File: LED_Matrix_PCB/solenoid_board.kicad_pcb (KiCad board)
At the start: 2 copper layers, 185 x 130 mm, 97 parts, among them J2 MCU_LEFT_LEGS, J3 MCU_RIGHT_LEGS

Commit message: Forgot to close files before pushing.
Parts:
- removed +5V_IN1: MCU_PWR_Supply, TerminalBlock:TerminalBlock_bornier-2_P5.08mm
- removed LED0_7, LED0_8, LED1_7, LED1_8, LED2_7, LED2_8, LED3_7, LED3_8, LED4_7, LED4_8, LED5_7, LED5_8, LED6_7, LED6_8, LED7_0, LED7_1, LED7_2, LED7_3, LED7_4, LED7_5, LED7_6, LED7_7, LED7_8: Screw-terminal, TerminalBlock:TerminalBlock_bornier-2_P5.08mm
- removed R330, R331, R332: 330, Resistor_THT:R_Axial_DIN0309_L9.0mm_D3.2mm_P20.32mm_Horizontal
- removed R333, R334, R335, R336, R337, R338: R, Resistor_THT:R_Axial_DIN0309_L9.0mm_D3.2mm_P20.32mm_Horizontal
- removed REF** (x4): MountingHole_2.7mm_M2.5, MountingHole:MountingHole_2.7mm_M2.5
- removed RJ0, RJ1: RJ45, Connector_RJ:RJ45_Amphenol_54602-x08_Horizontal
- added +5VIN1: Conn_01x02, Connector_PinHeader_2.54mm:PinHeader_1x02_P2.54mm_Vertical, F.Cu at (132.2, 74.0)
- added COMMS0: Conn_01x02, Connector_PinHeader_2.54mm:PinHeader_1x02_P2.54mm_Vertical, F.Cu at (103.2, 89.7)
- added COMMS1: Conn_01x02, Connector_PinHeader_2.54mm:PinHeader_1x02_P2.54mm_Vertical, F.Cu at (86.9, 108.6)
- added FET0: 2N7000, digikey-footprints:TO-92-3, F.Cu at (148.4, 89.1)
- added FET1: 2N7000, digikey-footprints:TO-92-3, F.Cu at (156.5, 81.9)
- added FET10: 2N7000, digikey-footprints:TO-92-3, F.Cu at (150.4, 99.7)
- added FET11: 2N7000, digikey-footprints:TO-92-3, F.Cu at (138.9, 114.1)
- added FET12: 2N7000, digikey-footprints:TO-92-3, F.Cu at (145.8, 108.8)
- added FET13: 2N7000, digikey-footprints:TO-92-3, F.Cu at (157.3, 97.8)
- added FET2: 2N7000, digikey-footprints:TO-92-3, F.Cu at (136.7, 103.5)
- added FET3: 2N7000, digikey-footprints:TO-92-3, F.Cu at (132.1, 110.7)
- added FET4: 2N7000, digikey-footprints:TO-92-3, F.Cu at (148.4, 94.4)
- added FET5: 2N7000, digikey-footprints:TO-92-3, F.Cu at (156.5, 87.2)
- added FET6: 2N7000, digikey-footprints:TO-92-3, F.Cu at (143.6, 103.5)
- added FET7: 2N7000, digikey-footprints:TO-92-3, F.Cu at (138.9, 108.8)
- added FET8: 2N7000, digikey-footprints:TO-92-3, F.Cu at (155.2, 92.5)
- added FET9: 2N7000, digikey-footprints:TO-92-3, F.Cu at (91.4, 114.3)
- added R10k0: 10k, Resistor_THT:R_Axial_DIN0204_L3.6mm_D1.6mm_P5.08mm_Vertical, F.Cu at (86.2, 95.3)
- added R10k1: 10k, Resistor_THT:R_Axial_DIN0204_L3.6mm_D1.6mm_P5.08mm_Vertical, F.Cu at (110.6, 73.2)
- added R10k10: 10k, Resistor_THT:R_Axial_DIN0204_L3.6mm_D1.6mm_P5.08mm_Vertical, F.Cu at (86.2, 82.7)
- added R10k11: 10k, Resistor_THT:R_Axial_DIN0204_L3.6mm_D1.6mm_P5.08mm_Vertical, F.Cu at (94.3, 76.4)
- added R10k12: 10k, Resistor_THT:R_Axial_DIN0204_L3.6mm_D1.6mm_P5.08mm_Vertical, F.Cu at (86.2, 79.5)
- added R10k13: 10k, Resistor_THT:R_Axial_DIN0204_L3.6mm_D1.6mm_P5.08mm_Vertical, F.Cu at (94.3, 73.2)
- added R10k2: 10k, Resistor_THT:R_Axial_DIN0204_L3.6mm_D1.6mm_P5.08mm_Vertical, F.Cu at (86.2, 76.4)
- added R10k3: 10k, Resistor_THT:R_Axial_DIN0204_L3.6mm_D1.6mm_P5.08mm_Vertical, F.Cu at (86.2, 73.2)
- added R10k4: 10k, Resistor_THT:R_Axial_DIN0204_L3.6mm_D1.6mm_P5.08mm_Vertical, F.Cu at (86.2, 89.0)
- added R10k5: 10k, Resistor_THT:R_Axial_DIN0204_L3.6mm_D1.6mm_P5.08mm_Vertical, F.Cu at (94.3, 82.7)
- added R10k6: 10k, Resistor_THT:R_Axial_DIN0204_L3.6mm_D1.6mm_P5.08mm_Vertical, F.Cu at (102.4, 76.4)
- added R10k7: 10k, Resistor_THT:R_Axial_DIN0204_L3.6mm_D1.6mm_P5.08mm_Vertical, F.Cu at (94.3, 79.5)
- added R10k8: 10k, Resistor_THT:R_Axial_DIN0204_L3.6mm_D1.6mm_P5.08mm_Vertical, F.Cu at (86.2, 85.8)
- added R10k9: 10k, Resistor_THT:R_Axial_DIN0204_L3.6mm_D1.6mm_P5.08mm_Vertical, F.Cu at (102.4, 73.2)
- added R300: 300, Resistor_THT:R_Axial_DIN0204_L3.6mm_D1.6mm_P5.08mm_Vertical, F.Cu at (110.6, 79.5)
- added R301: 300, Resistor_THT:R_Axial_DIN0204_L3.6mm_D1.6mm_P5.08mm_Vertical, F.Cu at (102.4, 85.8)
- added R302: 300, Resistor_THT:R_Axial_DIN0204_L3.6mm_D1.6mm_P5.08mm_Vertical, F.Cu at (86.2, 101.6)
- added R303: 300, Resistor_THT:R_Axial_DIN0204_L3.6mm_D1.6mm_P5.08mm_Vertical, F.Cu at (86.2, 92.1)
- added R304: 300, Resistor_THT:R_Axial_DIN0204_L3.6mm_D1.6mm_P5.08mm_Vertical, F.Cu at (86.2, 104.7)
- added R305: 300, Resistor_THT:R_Axial_DIN0204_L3.6mm_D1.6mm_P5.08mm_Vertical, F.Cu at (94.3, 95.3)
- added R306: 300, Resistor_THT:R_Axial_DIN0204_L3.6mm_D1.6mm_P5.08mm_Vertical, F.Cu at (118.7, 73.2)
- added R307: 300, Resistor_THT:R_Axial_DIN0204_L3.6mm_D1.6mm_P5.08mm_Vertical, F.Cu at (94.3, 92.1)
- added R308: 300, Resistor_THT:R_Axial_DIN0204_L3.6mm_D1.6mm_P5.08mm_Vertical, F.Cu at (86.2, 98.4)
- added R309: 300, Resistor_THT:R_Axial_DIN0204_L3.6mm_D1.6mm_P5.08mm_Vertical, F.Cu at (94.3, 89.0)
- added R310: 300, Resistor_THT:R_Axial_DIN0204_L3.6mm_D1.6mm_P5.08mm_Vertical, F.Cu at (102.4, 82.7)
- added R311: 300, Resistor_THT:R_Axial_DIN0204_L3.6mm_D1.6mm_P5.08mm_Vertical, F.Cu at (110.6, 76.4)
- added R312: 300, Resistor_THT:R_Axial_DIN0204_L3.6mm_D1.6mm_P5.08mm_Vertical, F.Cu at (102.4, 79.5)
- added R313: 300, Resistor_THT:R_Axial_DIN0204_L3.6mm_D1.6mm_P5.08mm_Vertical, F.Cu at (94.3, 85.8)
- GND1: value Conn_01x01_Male -> Conn_01x01
- LED0_0, LED0_1, LED0_2, LED0_3, LED0_4, LED0_5, LED0_6, LED1_0, LED1_1, LED1_2, LED1_3, LED1_4, LED1_5, LED1_6, LED2_0, LED2_1, LED2_2, LED2_3, LED2_4, LED2_5, LED2_6, LED3_0, LED3_1, LED3_2, LED3_3, LED3_4, LED3_5, LED3_6, LED4_0, LED4_1, LED4_2, LED4_3, LED4_4, LED4_5, LED4_6, LED5_0, LED5_1, LED5_2, LED5_3, LED5_4, LED5_5, LED5_6, LED6_0, LED6_1, LED6_2, LED6_3, LED6_4, LED6_5, LED6_6: value Screw-terminal -> Conn_01x02; footprint TerminalBlock:TerminalBlock_bornier-2_P5.08mm -> Connector_PinHeader_2.54mm:PinHeader_1x02_P2.54mm_Vertical
- R10, R11: footprint Resistor_THT:R_Axial_DIN0309_L9.0mm_D3.2mm_P20.32mm_Horizontal -> Resistor_THT:R_Axial_DIN0204_L3.6mm_D1.6mm_P7.62mm_Horizontal
- moved GND1 118.1 mm to (98.4, 113.6)
- moved LED0_0 99.9 mm to (160.1, 74.0)
- moved LED6_2 82.5 mm to (150.8, 74.0)
- moved LED5_0 77.5 mm to (136.9, 95.6)
- moved LED5_1 74.6 mm to (143.9, 88.4)
- moved LED4_0 71.9 mm to (127.6, 74.0)
- moved LED5_3 70.1 mm to (155.5, 74.0)
- moved LED0_1 68.4 mm to (118.3, 110.0)
- moved LED1_1 68.2 mm to (141.5, 74.0)
- moved LED4_1 67.2 mm to (139.2, 88.4)
- moved LED6_1 65.4 mm to (132.3, 95.6)
- moved LED2_1 63.7 mm to (136.9, 74.0)
- moved LED1_0 62.6 mm to (118.3, 95.6)
- moved LED0_2 61.6 mm to (142.7, 81.2)
- moved LED4_2 56.5 mm to (141.6, 95.6)
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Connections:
- net /RJ45_4 renamed /A
- net /RJ45_5 renamed /B
- J2 pad 11: /ROW6 -> (no net)
- J2 pad 12: /MOSI -> (no net)
- J3 pad 11: /SCL -> (no net)
- J3 pad 12: /SDA -> (no net)
- LED0_0 pad 2: /A0 -> /ROW0
- LED0_1 pad 2: /A0 -> /ROW0
- LED0_2 pad 2: /A0 -> /ROW0
- LED0_3 pad 2: /A0 -> /ROW0
- LED0_4 pad 2: /A0 -> /ROW0
- LED0_5 pad 2: /A0 -> /ROW0
- LED0_6 pad 2: /A0 -> /ROW0
- LED1_0 pad 2: /A1 -> /ROW1
- LED1_1 pad 2: /A1 -> /ROW1
- LED1_2 pad 2: /A1 -> /ROW1
- LED1_3 pad 2: /A1 -> /ROW1
- LED1_4 pad 2: /A1 -> /ROW1
- LED1_5 pad 2: /A1 -> /ROW1
- LED1_6 pad 2: /A1 -> /ROW1
- LED2_0 pad 2: /A2 -> /ROW2
- LED2_1 pad 2: /A2 -> /ROW2
- LED2_2 pad 2: /A2 -> /ROW2
- LED2_3 pad 2: /A2 -> /ROW2
- LED2_4 pad 2: /A2 -> /ROW2
- LED2_5 pad 2: /A2 -> /ROW2
- LED2_6 pad 2: /A2 -> /ROW2
- LED3_0 pad 2: /A3 -> /ROW3
- LED3_1 pad 2: /A3 -> /ROW3
- LED3_2 pad 2: /A3 -> /ROW3
- LED3_3 pad 2: /A3 -> /ROW3
- LED3_4 pad 2: /A3 -> /ROW3
- LED3_5 pad 2: /A3 -> /ROW3
- LED3_6 pad 2: /A3 -> /ROW3
- LED4_0 pad 2: /A4 -> /ROW4
- LED4_1 pad 2: /A4 -> /ROW4
- LED4_2 pad 2: /A4 -> /ROW4
- LED4_3 pad 2: /A4 -> /ROW4
- LED4_4 pad 2: /A4 -> /ROW4
- LED4_5 pad 2: /A4 -> /ROW4
- LED4_6 pad 2: /A4 -> /ROW4
- LED5_0 pad 2: /A5 -> /ROW5
- LED5_1 pad 2: /A5 -> /ROW5
- LED5_2 pad 2: /A5 -> /ROW5
- LED5_3 pad 2: /A5 -> /ROW5
- LED5_4 pad 2: /A5 -> /ROW5
- LED5_5 pad 2: /A5 -> /ROW5
- LED5_6 pad 2: /A5 -> /ROW5
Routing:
- net /A0: track 179.2 -> 0.00 mm
- net /MOSI: track 174.9 -> 0.00 mm
- net /D13: track 172.9 -> 0.00 mm
- net /A1: track 168.7 -> 0.00 mm
- net /ROW6: track 165.6 -> 0.00 mm
- net /A2: track 163.1 -> 0.00 mm
- net /D12: track 162.2 -> 0.00 mm
- net /A4: track 160.5 -> 0.00 mm
- net /A5: track 160.3 -> 0.00 mm
- net /A3: track 159.7 -> 0.00 mm
- net /D11: track 156.4 -> 0.00 mm
- net /D10: track 144.7 -> 0.00 mm
- net /D9: track 131.6 -> 0.00 mm
- net /D6: track 119.4 -> 0.00 mm
- net /D5: track 106.7 -> 0.00 mm
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- removed copper zone on B.Cu, net GND
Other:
- board outline removed
- board text added: "02/23/2020"
- board text added: "LED Matrix Board V2.0"
- board text removed: "02/07/2020"
- board text removed: "LED Matrix Board V1.0"

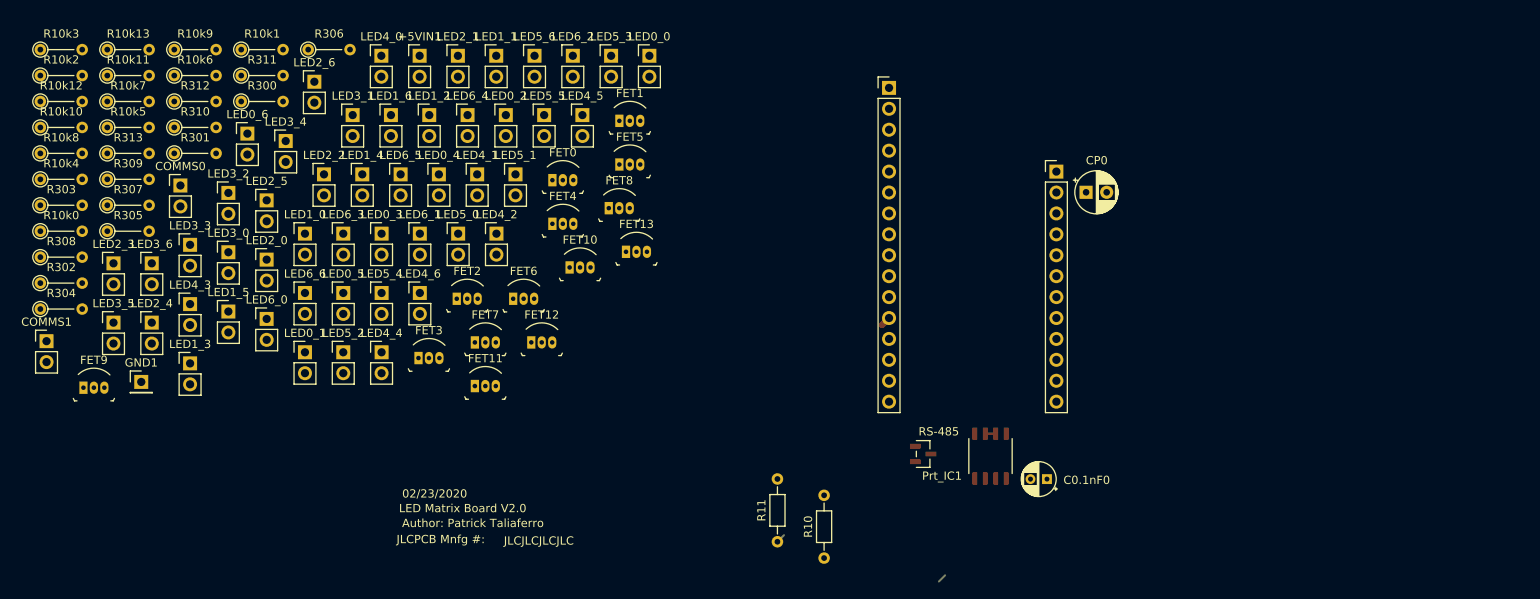
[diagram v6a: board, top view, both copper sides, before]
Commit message: Fixed the connections of the downstream MOSFETS. WOrked on geometry, sorted out footprints.
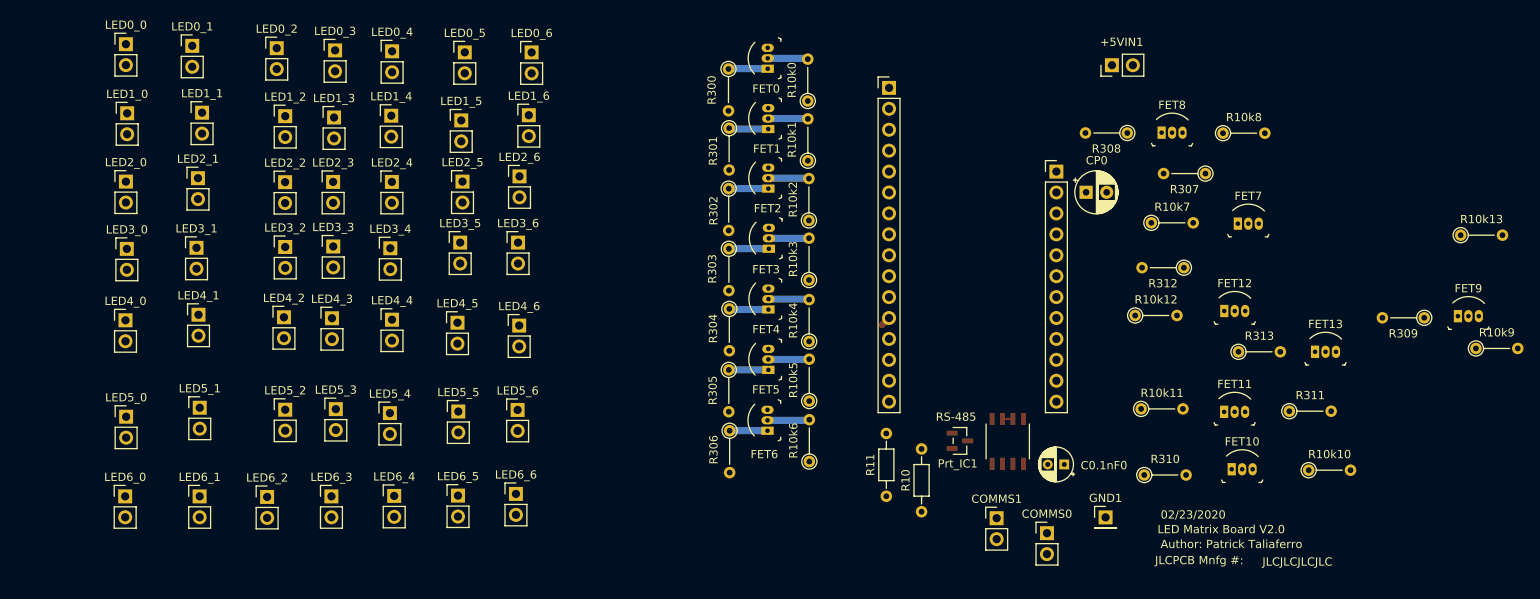
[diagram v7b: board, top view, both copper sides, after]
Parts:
- moved FET9 167.1 mm to (258.3, 105.6)
- moved R10k13 165.9 mm to (258.6, 95.7)
- moved R10k9 162.2 mm to (260.5, 109.5)
- moved R309 160.8 mm to (254.2, 105.8), turned to 180 degrees
- moved R10k10 159.5 mm to (240.2, 124.3)
- moved R10k8 143.6 mm to (229.8, 83.4)
- moved R313 139.4 mm to (231.7, 109.9)
- moved R10k12 135.4 mm to (219.1, 105.5)
- moved R311 133.6 mm to (237.8, 117.1)
- moved R307 133.4 mm to (227.6, 88.3), turned to 180 degrees
- moved R308 132.8 mm to (218.2, 83.3), turned to 180 degrees
- moved R10k11 131.9 mm to (219.8, 116.8)
- moved R10k7 127.6 mm to (221.1, 94.2)
- moved R310 125.1 mm to (220.2, 124.9)
- moved R312 124.2 mm to (225.0, 99.7), turned to 180 degrees
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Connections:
- FET10 pad 3: +5V -> /COL3
- FET11 pad 3: +5V -> /COL4
- FET12 pad 3: +5V -> /COL5
- FET13 pad 3: +5V -> /COL6
- FET7 pad 3: +5V -> /COL0
- FET8 pad 3: +5V -> /COL1
- FET9 pad 3: +5V -> /COL2
- R307 pad 2: /COL0 -> GND
- R308 pad 2: /COL1 -> GND
- R309 pad 2: /COL2 -> GND
- R310 pad 2: /COL3 -> GND
- R311 pad 2: /COL4 -> GND
- R312 pad 2: /COL5 -> GND
- R313 pad 2: /COL6 -> GND
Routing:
- net Net-(FET6-Pad2): track 0.00 -> 5.11 mm
- net Net-(FET5-Pad2): track 0.00 -> 4.98 mm
- net Net-(FET4-Pad2): track 0.00 -> 4.97 mm
- net Net-(FET2-Pad2): track 0.00 -> 4.95 mm
- net Net-(FET0-Pad2): track 0.00 -> 4.91 mm
- net Net-(FET3-Pad2): track 0.00 -> 4.88 mm
- net Net-(FET3-Pad1): track 0.00 -> 4.85 mm
- net Net-(FET1-Pad2): track 0.00 -> 4.83 mm
- net Net-(FET2-Pad1): track 0.00 -> 4.81 mm
- net Net-(FET5-Pad1): track 0.00 -> 4.80 mm
- net Net-(FET1-Pad1): track 0.00 -> 4.79 mm
- net Net-(FET4-Pad1): track 0.00 -> 4.78 mm
- net Net-(FET0-Pad1): track 0.00 -> 4.77 mm
- net Net-(FET6-Pad1): track 0.00 -> 4.60 mm
- net /B: track 2.19 -> 0.00 mm
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
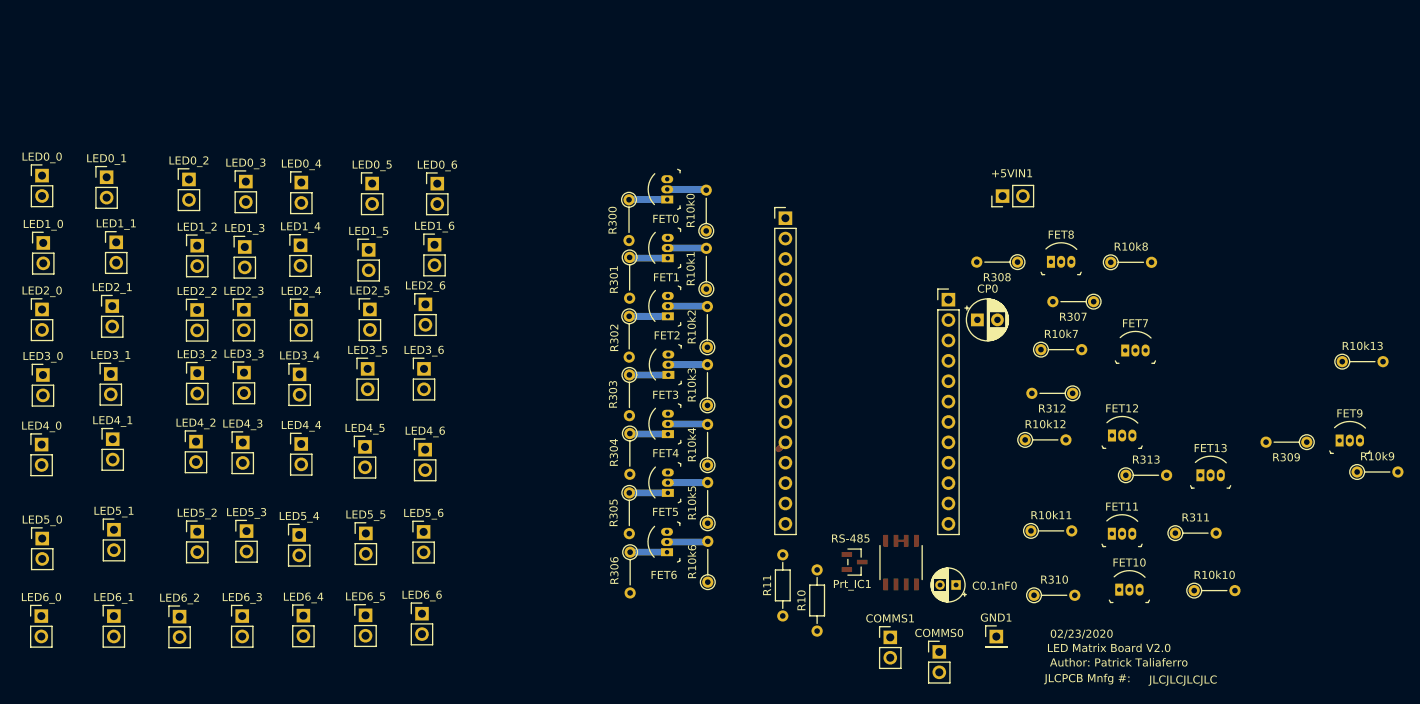
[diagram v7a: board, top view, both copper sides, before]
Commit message: Cleaned geometry on layout. Routed a number of wires. Only a little bit of routing left.
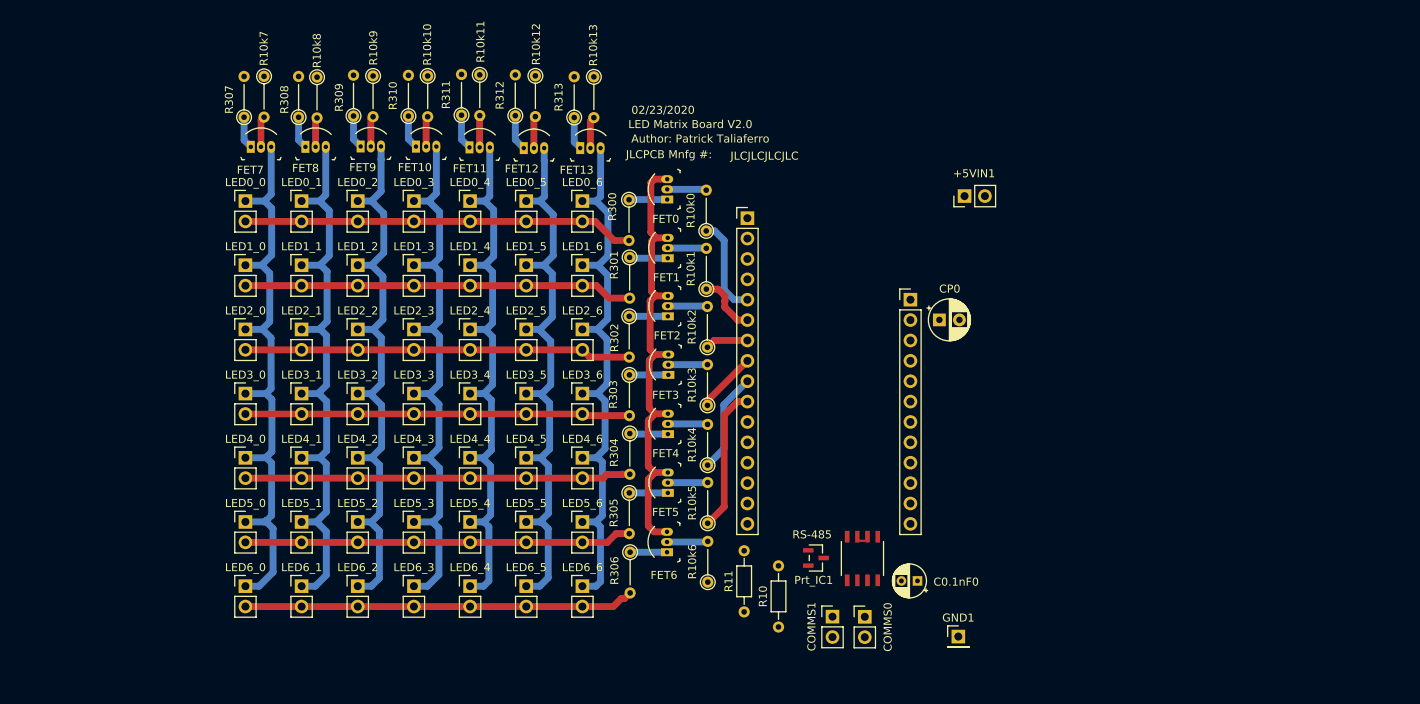
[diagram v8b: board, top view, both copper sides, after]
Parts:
- moved R10k9 132.2 mm to (137.8, 60.1), turned to 270 degrees
- moved FET9 127.4 mm to (136.3, 68.9)
- moved R309 125.6 mm to (135.4, 65.1), turned to 90 degrees
- moved R10k10 115.1 mm to (144.6, 60.1), turned to 270 degrees
- moved FET7 111.9 mm to (122.6, 69.0)
- moved R307 108.4 mm to (121.8, 65.3), turned to 90 degrees
- moved FET10 103.6 mm to (143.2, 68.9)
- moved R311 103.1 mm to (148.9, 65.0), turned to 90 degrees
- moved R10k7 102.7 mm to (124.2, 60.2), turned to 270 degrees
- moved R10k8 101.6 mm to (130.8, 60.3), turned to 270 degrees
- moved R10k13 99.8 mm to (165.4, 60.2), turned to 270 degrees
- moved R310 98.2 mm to (142.2, 65.1), turned to 90 degrees
- moved FET8 94.0 mm to (129.4, 69.0)
- moved FET11 93.4 mm to (149.8, 69.0)
- moved R308 91.4 mm to (128.5, 65.3), turned to 90 degrees
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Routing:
- net /COL0: track 0.00 -> 75.8 mm
- net /COL1: track 0.00 -> 75.0 mm
- net /COL3: track 0.00 -> 75.0 mm
- net /COL5: track 0.00 -> 73.6 mm
- net /COL2: track 0.00 -> 73.6 mm
- net /COL6: track 0.00 -> 72.6 mm
- net /COL4: track 0.00 -> 72.1 mm
- net +5V: track 0.00 -> 58.5 mm
- net /ROW0: track 0.00 -> 48.8 mm
- net /ROW6: track 0.00 -> 48.7 mm
- net /ROW1: track 0.00 -> 48.5 mm
- net /ROW5: track 0.00 -> 48.3 mm
- net /ROW2: track 0.00 -> 48.2 mm
- net /ROW4: track 0.00 -> 48.1 mm
- net /ROW3: track 0.00 -> 47.9 mm
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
